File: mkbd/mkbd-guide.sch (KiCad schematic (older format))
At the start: 8 parts, among them SW1 RST, SW2 SW_PUSH, SW3 SW_PUSH, SW4 SW_PUSH, SW5 SW_PUSH, SW6 SW_PUSH, SW7 SW_PUSH, U1 ProMicro_r

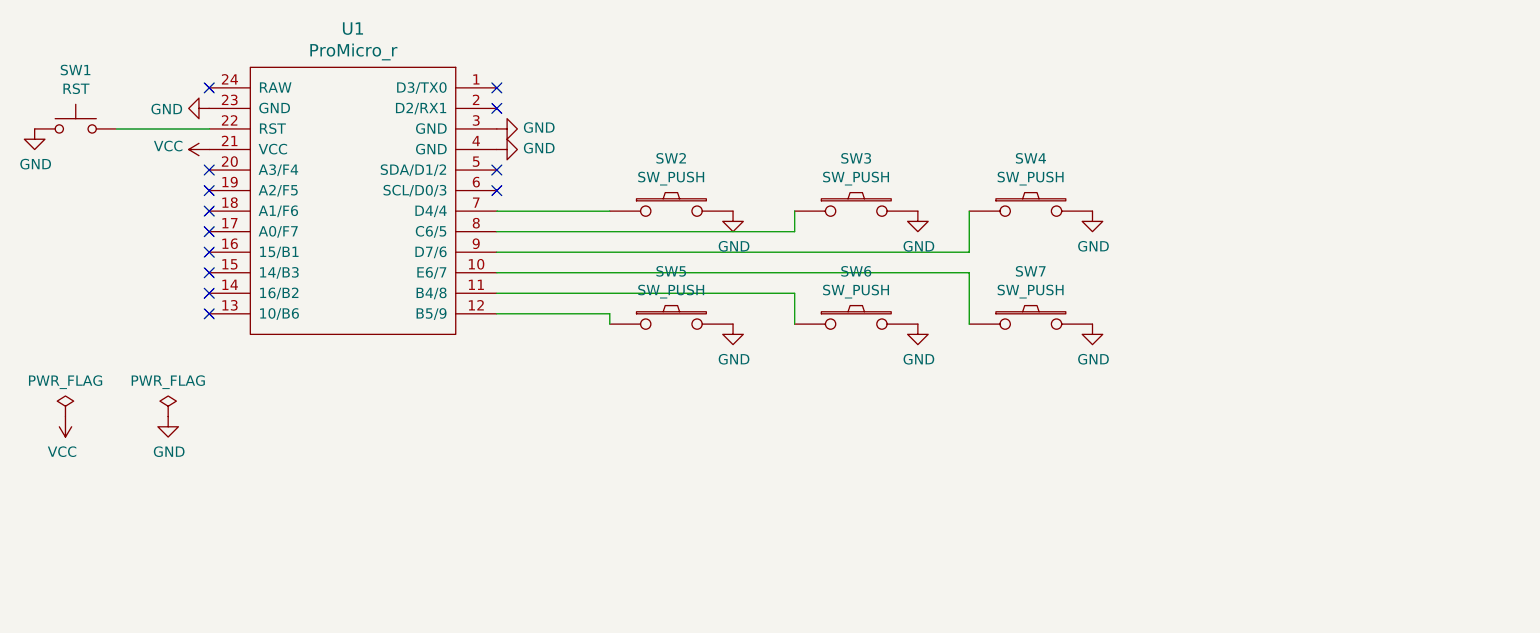
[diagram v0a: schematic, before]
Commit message: Added silkscreen and gerbers
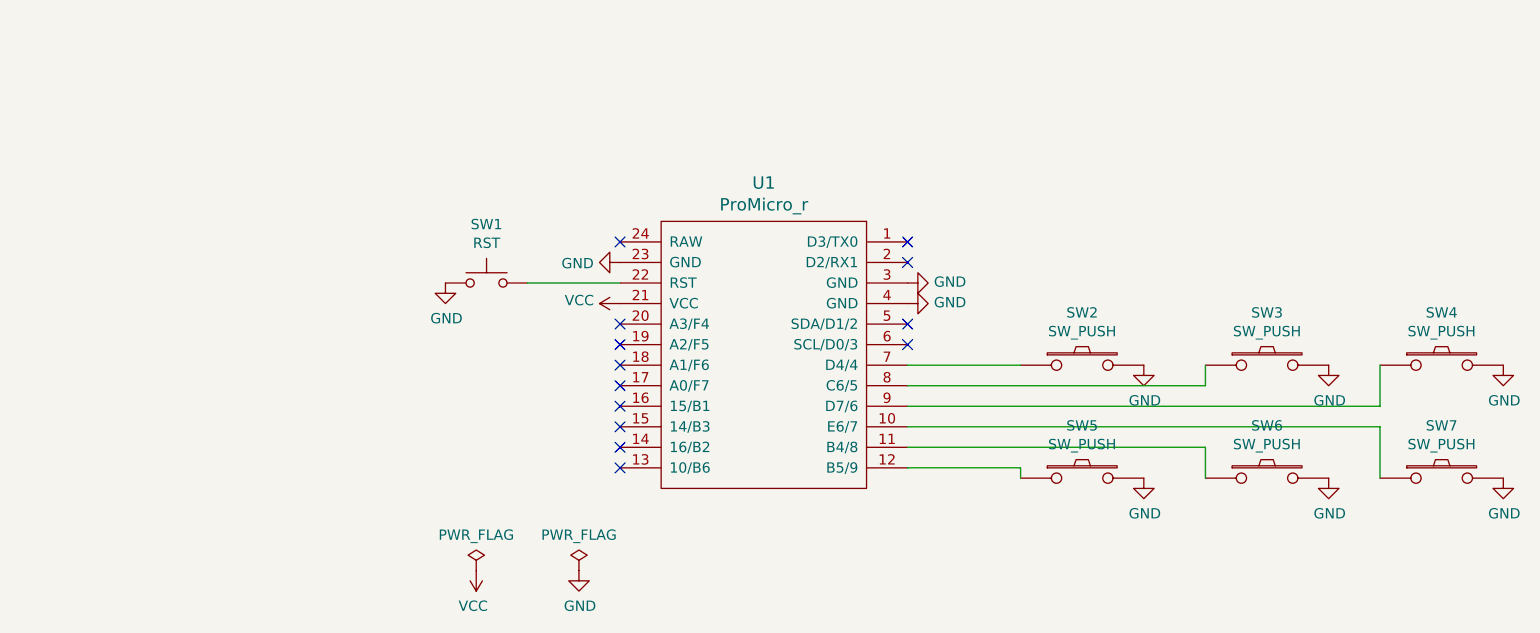
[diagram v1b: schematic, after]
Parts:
- SW1: footprint kbd:ResetSW_4 -> kbd:ResetSW
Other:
- moved on the sheet: SW1, SW2, SW3, SW4, SW5, SW6, SW7, U1
